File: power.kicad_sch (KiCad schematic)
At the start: 17 parts, among them J3 Conn_01x02, Q1 CSD17575Q3, Q2 CSD17575Q3, U19 LM74502, U7 AMS1117-3.3, U8 AMS1117-5.0

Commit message: remove unneeded stuff
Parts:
- removed D11: D_Schottky, Diode_SMD:D_SOD-123, symbol Device:D_Schottky
- removed Q2: CSD17575Q3, beavs-footprints:SON-8-1EP-3.3x3.3mm-nexfet, symbol Transistor_FET:Q_NMOS_SSSGD_AvalancheRated
- removed R15: 5.1k, Resistor_SMD:R_0402_1005Metric, symbol Device:R_Small
- removed R2: 300, Resistor_SMD:R_1206_3216Metric, symbol Device:R
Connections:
- net EN is gone; now on an unnamed net: U19.1 (EN/UVLO)
- net +BATT: now also Q1.1 (S), Q1.2 (S), Q1.3 (S), U19.8 (SRC)
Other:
- note removed: "1206"
- note removed: "Reverse polarity protection Disabled until capacitors charged"
- note removed: "Slow charge capacitors"
- moved on the sheet: C15, C16, C17, C18, C45, C46, D7, D8, J3, Q1, U19, U7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

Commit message: changes!
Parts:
- removed C45, C46: 220n, Capacitor_SMD:C_0402_1005Metric, symbol Device:C_Small
- removed Q1: CSD17575Q3, beavs-footprints:SON-8-1EP-3.3x3.3mm-nexfet, symbol Transistor_FET:Q_NMOS_SSSGD_AvalancheRated
- removed U19: LM74502, beavs-footprints:SOT-23-8-THIN, symbol beavs-symbols:LM74502
- added U4: TPS25983, beavs-footprints:Texas_RGE0024M_QFN-24_4x4_Pitch0.5mm_2EP, symbol beavs-symbols:TPS25983
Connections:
- net +BATT: now also U4.[17,18,19,20,21,22,23,24] (OUT)
- net GND: now also U4.[4,5,14,26] (GND)
- net at D7.2 (A), J3.2 (Pin_2): now also U4.[1,2,3,16,25] (IN)

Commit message: relayout and route
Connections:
- net GND: now also U4.12 (OVLO)
- net VDD: now reaches D7.2 (A), J3.2 (Pin_2), U4.[1,2,3,16,25] (IN)
- net EN: now reaches U4.6 (EN/UVLO)
- no-connect marks 0 -> 1
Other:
- note added: "6.4-8.4V"
- note removed: "-8.4-8.4V 6.4-8.4V in operation"
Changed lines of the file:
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@@
 		)
 	)
-	(text "-8.4-8.4V\n6.4-8.4V in operation"
+	(text "6.4-8.4V"
 		(exclude_from_sim no)
 		(at 61.976 60.198 0)
@@
 		(color 0 0 0 0)
 	)
+	(no_connect
+		(at 220.98 68.58)
+	)
 	(wire
 		(pts
@@
 	(wire
 		(pts
+			(xy 182.88 72.39) (xy 182.88 76.2)
+		)
+		(stroke
+			(width 0)
+			(type default)
+		)
+	)
+	(wire
+		(pts
 			(xy 78.74 139.7) (xy 78.74 104.14)
 		)
@@
 	(wire
 		(pts
+			(xy 88.9 62.23) (xy 88.9 63.5)
+		)
+		(stroke
+			(width 0)
+			(type default)
+		)
+	)
+	(wire
+		(pts
 			(xy 69.85 90.17) (xy 68.58 90.17)
 		)
@@
 			(width 0)
 			(type default)
+		)
+	)
+	(wire
+		(pts
+			(xy 180.34 68.58) (xy 190.5 68.58)
+		)
+		(stroke
+			(width 0)
+			(type default)
+		)
+	)
+	(wire
+		(pts
+			(xy 190.5 72.39) (xy 182.88 72.39)
+		)
+		(stroke
+			(width 0)
+			(type default)
+		)
+	)
+	(hierarchical_label "EN"
+		(shape input)
+		(at 180.34 68.58 180)
+		(effects
+			(font
+				(size 1.27 1.27)
+			)
+			(justify right)
 		)
 	)
@@
 	(symbol
 		(lib_id "power:GND")
+		(at 182.88 76.2 0)
+		(unit 1)
+		(body_style 1)
+		(exclude_from_sim no)
+		(in_bom yes)
+		(on_board yes)
+		(in_pos_files yes)
+		(dnp no)
+		(fields_autoplaced yes)
+		(property "Reference" "#PWR09"
+			(at 182.88 82.55 0)
+			(hide yes)
+			(show_name no)
+			(do_not_autoplace no)
+			(effects
+				(font
+					(size 1.27 1.27)
+				)
+			)
+		)
+		(property "Value" "GND"
+			(at 182.88 81.28 0)
+			(show_name no)
+			(do_not_autoplace no)
+			(effects
+				(font
+					(size 1.27 1.27)
+				)
+			)
+		)
+		(property "Footprint" ""
+			(at 182.88 76.2 0)
+			(hide yes)
+			(show_name no)
+			(do_not_autoplace no)
+			(effects
+				(font
+					(size 1.27 1.27)
+				)
+			)
+		)
+		(property "Datasheet" ""
+			(at 182.88 76.2 0)
+			(hide yes)
+			(show_name no)
+			(do_not_autoplace no)
+			(effects
+				(font
+					(size 1.27 1.27)
+				)
+			)
+		)
+		(property "Description" "Power symbol creates a global label with name \"GND\" , ground"
+			(at 182.88 76.2 0)
+			(hide yes)
+			(show_name no)
+			(do_not_autoplace no)
+			(effects
+				(font
+					(size 1.27 1.27)
+				)
+			)
+		)
+		(pin "1"
+		)
+		(instances
+			(project "beavs-6"
+				(path "/49232f62-a438-4b3e-9be5-c2b3074d8de1/43b34b82-cf9c-4554-a5be-2b816c03d018"
+					(reference "#PWR09")
+					(unit 1)
+				)
+			)
+		)
+	)
+	(symbol
+		(lib_id "power:GND")
 		(at 96.52 111.76 0)
 		(unit 1)
@@
 					(unit 1)
 				)
+			)
+		)
+	)
+	(symbol
+		(lib_id "power:VDD")
+		(at 88.9 62.23 0)
+		(unit 1)
+		(body_style 1)
+		(exclude_from_sim no)
+		(in_bom yes)
+		(on_board yes)
+		(in_pos_files yes)
+		(dnp no)
+		(fields_autoplaced yes)
+		(property "Reference" "#PWR015"
+			(at 88.9 66.04 0)
+			(hide yes)
+			(show_name no)
+			(do_not_autoplace no)
+			(effects
+				(font
+					(size 1.27 1.27)
+				)
+			)
+		)
+		(property "Value" "VDD"
+			(at 88.9 57.15 0)
+			(show_name no)
+			(do_not_autoplace no)
+			(effects
+				(font
+					(size 1.27 1.27)
+				)
+			)
+		)
+		(property "Footprint" ""
+			(at 88.9 62.23 0)
+			(hide yes)
+			(show_name no)
+			(do_not_autoplace no)
+			(effects
+				(font
+					(size 1.27 1.27)
+				)
+			)
+		)
+		(property "Datasheet" ""
+			(at 88.9 62.23 0)
+			(hide yes)
+			(show_name no)
+			(do_not_autoplace no)
+			(effects
+				(font
+					(size 1.27 1.27)
+				)
+			)
+		)
+		(property "Description" "Power symbol creates a global label with name \"VDD\""
+			(at 88.9 62.23 0)
+			(hide yes)
+			(show_name no)
+			(do_not_autoplace no)
+			(effects
+				(font
+					(size 1.27 1.27)
+				)
+			)
+		)
+		(pin "1"
+		)
+		(instances
+			(project "beavs-6"
+				(path "/49232f62-a438-4b3e-9be5-c2b3074d8de1/43b34b82-cf9c-4554-a5be-2b816c03d018"
+					(reference "#PWR015")
+					(unit 1)
+				)

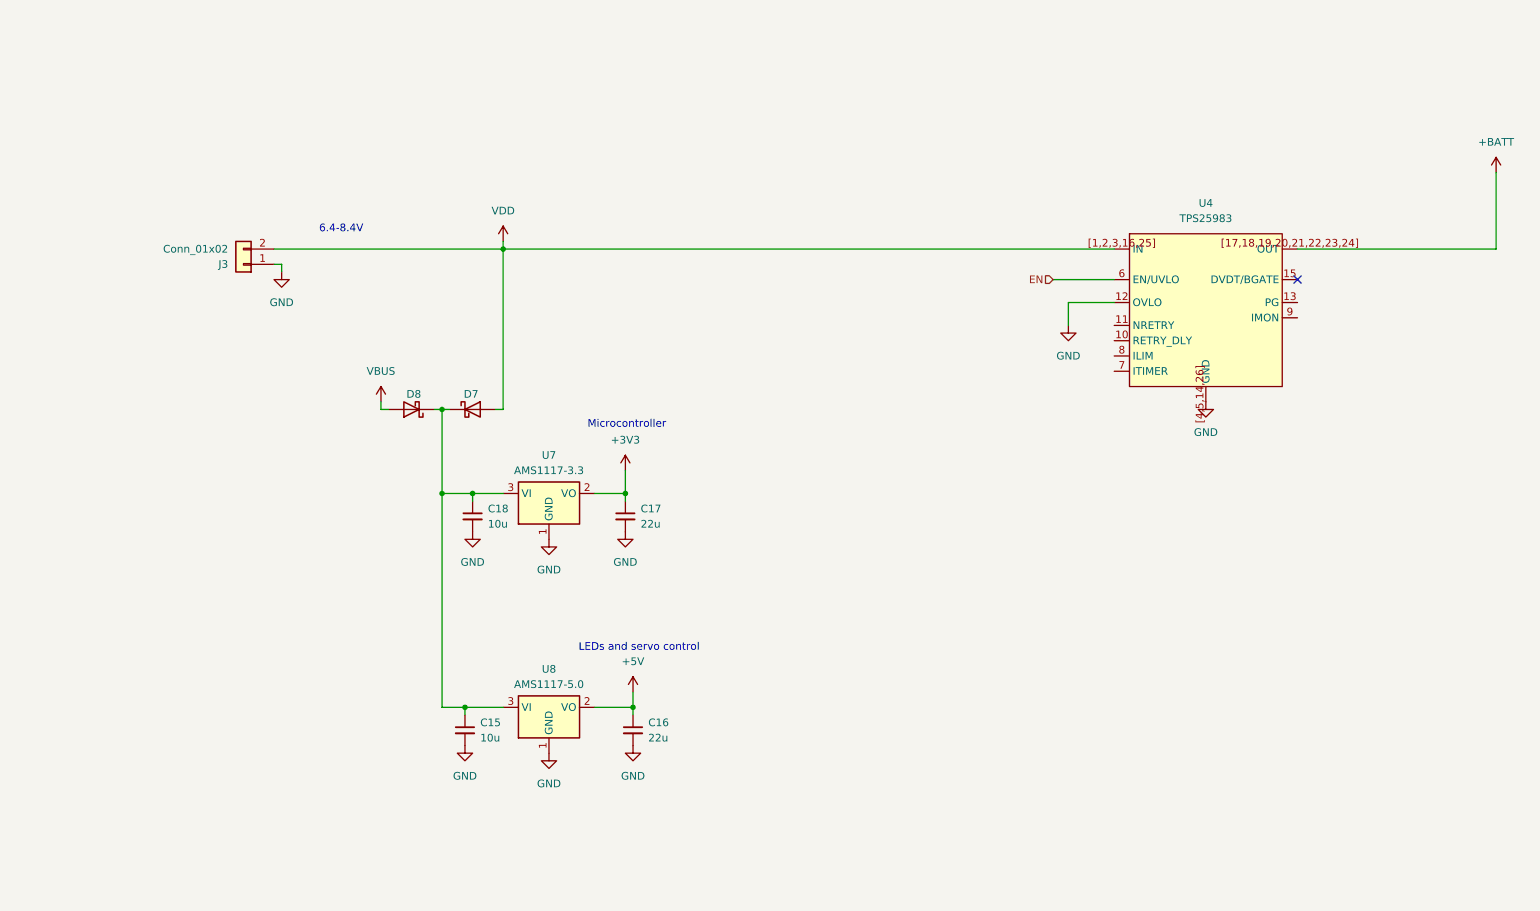
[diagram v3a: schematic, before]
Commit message: add reverse polarity protection
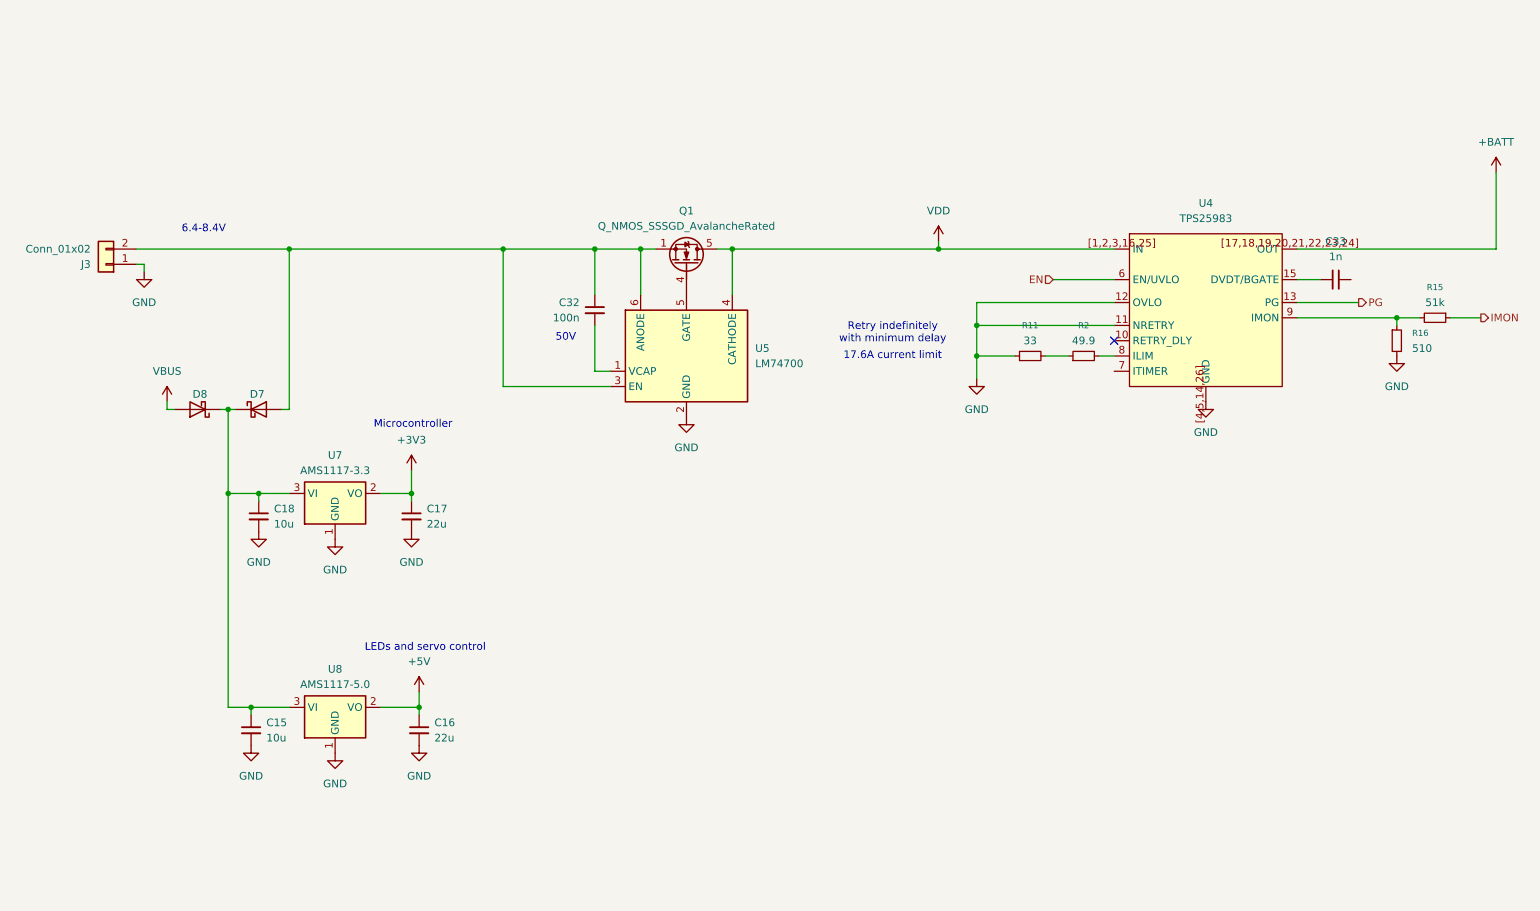
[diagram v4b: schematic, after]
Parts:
- added C32: 100n, Capacitor_SMD:C_0603_1608Metric, symbol Device:C_Small
- added C33: 1n, Capacitor_SMD:C_0402_1005Metric, symbol Device:C_Small
- added Q1: Q_NMOS_SSSGD_AvalancheRated, Package_SO:Vishay_PowerPAK_1212-8_Single, symbol Transistor_FET:Q_NMOS_SSSGD_AvalancheRated
- added R11: 33, Resistor_SMD:R_0402_1005Metric, symbol Device:R_Small
- added R15: 51k, Resistor_SMD:R_0402_1005Metric, symbol Device:R_Small
- added R16: 510, Resistor_SMD:R_0402_1005Metric, symbol Device:R_Small
- added R2: 49.9, Resistor_SMD:R_0402_1005Metric, symbol Device:R_Small
- added U5: LM74700, Package_TO_SOT_SMD:SOT-23-6, symbol Power_Management:LM74700
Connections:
- net GND: now also U4.11 (NRETRY), R11.1, R16.2, U5.2 (GND)
- net VDD: now also Q1.5 (D), U5.4 (CATHODE); no longer D7.2 (A), J3.2 (Pin_2)
- net PG: now reaches U4.13 (PG)
- net at U4.15 (DVDT/BGATE): now also C33.1
- net at U4.8 (ILIM): now also R2.2
- net at U4.9 (IMON): now also R15.2, R16.1
- new net: C32.1, D7.2 (A), J3.2 (Pin_2), Q1.1 (S), Q1.2 (S), Q1.3 (S), U5.3 (EN), U5.6 (ANODE)
- new net: R11.2, R2.1
- new net: Q1.4 (G), U5.5 (GATE)
- new net: C32.2, U5.1 (VCAP)
- new net IMON: R15.1
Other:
- note added: "17.6A current limit"
- note added: "50V"
- note added: "Retry indefinitely with minimum delay"
- moved on the sheet: C15, C16, C17, C18, D7, D8, J3, U7, U8

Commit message: restore symbols library, wire up PG and IMON, refine routing
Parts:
- added C34: TBD, Capacitor_SMD:C_0402_1005Metric, symbol Device:C_Small
- added C35: 10u, Capacitor_SMD:C_0603_1608Metric, symbol Device:C_Small
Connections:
- net GND: now also C33.1, C34.1, C35.2
- net VDD: now also D7.2 (A), C35.1
- net at C32.1, J3.2 (Pin_2), Q1.1 (S)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: no longer D7.2 (A)
- net at U4.15 (DVDT/BGATE): now also C33.2; no longer C33.1
- net at U4.7 (ITIMER): now also C34.2
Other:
- note added: "3A inrush"
- moved on the sheet: C15, C16, C17, C18, C32, D7, D8, Q1, R15, R16, U5, U7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
